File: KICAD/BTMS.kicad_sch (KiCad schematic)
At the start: 151 parts, among them J1 Batt_Ballance, J2 AUX_Charge, J3 Battery_IO, J4 Power_Out, J5 BT_LM62, J6 DSKY, J7 PWR_SW, J8 ICSP, J9 Heater, P1 USB_C_Plug, Q1 SSM3K341R, Q2 DMN65D8L, Q3 SSM3K341R, Q4 FDN340P, Q5 FDN340P, Q6 FDN340P, Q7 DMN65D8L, Q8 DMN65D8L, U1 ACS711xLCTR-25AB, U10 BA033CC0FP-E2, U11 AON7522E, U12 AON7522E, U13 LM62CIM3/NOPB, U14 FAN3100TSX, U15 FAN3100TSX, U16 AON7522E, U17 dsPIC30F3011-PT, U18 FT230XQ, U2 AP33771, U3 IS281-4, U4 Q294700DSGR, U5 SCF4030-12-0X, U6 AONR21321, U7 ACS711xLCTR-25AB, U8 IS281-4, U9 IRS2184

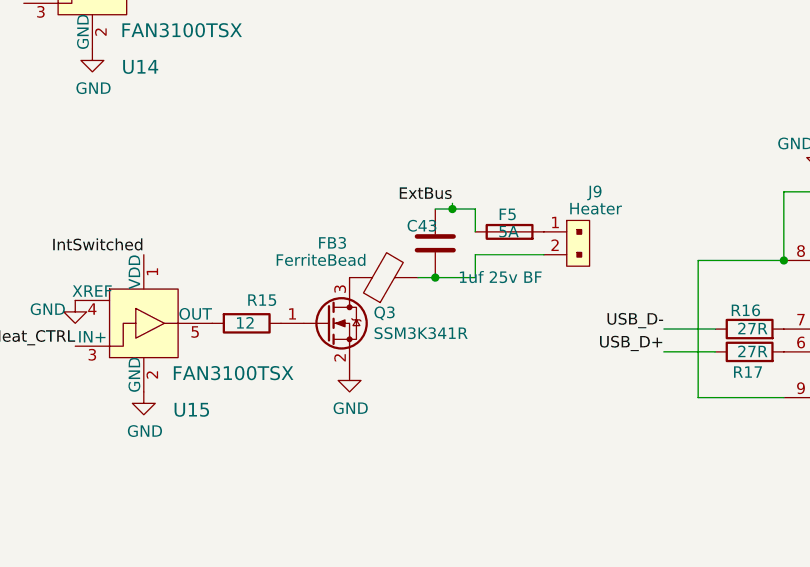
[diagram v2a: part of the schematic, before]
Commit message: Extended board and placed mounting points.
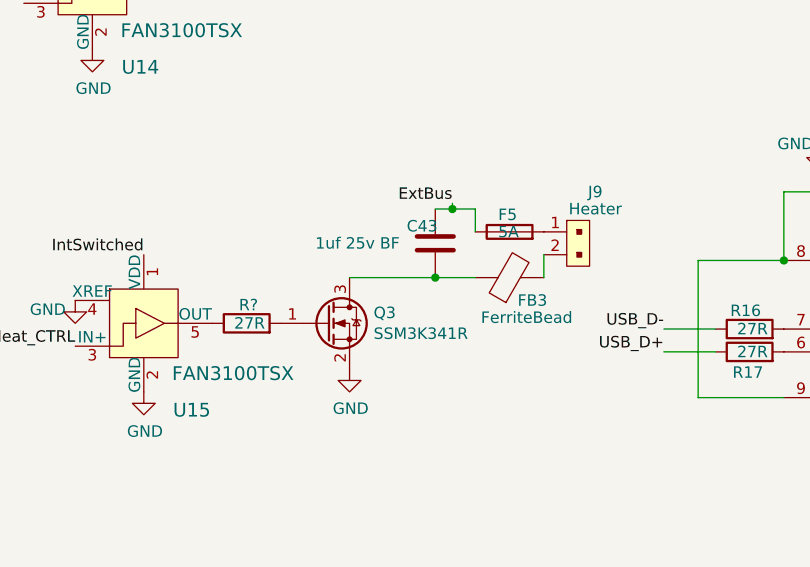
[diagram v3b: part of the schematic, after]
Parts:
- removed R15: 12, Resistor_SMD:R_0603_1608Metric, symbol Device:R
- added R?: 27R, Resistor_SMD:R_0603_1608Metric, symbol Device:R
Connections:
- net at FB3.2, J9.2: no longer C43.2
- net at U15.5 (OUT): now also R?.1
- net at Q3.1 (G): now also R?.2
- net at FB3.1, Q3.3 (D): now also C43.2
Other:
- moved on the sheet: FB3
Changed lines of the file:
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@@
   (junction (at 271.78 39.37) (diameter 0) (color 0 0 0 0)
   )
+  (junction (at 293.37 103.505) (diameter 0) (color 0 0 0 0)
+  )
   (junction (at 249.555 210.185) (diameter 0) (color 0 0 0 0)
   )
@@
   (junction (at 92.71 67.945) (diameter 0) (color 0 0 0 0)
   )
-  (junction (at 293.37 103.505) (diameter 0) (color 0 0 0 0)
-  )
   (junction (at 218.44 208.28) (diameter 0) (color 0 0 0 0)
   )
@@
     (stroke (width 0) (type default) (color 0 0 0 0))
   )
-  (wire (pts (xy 293.37 103.505) (xy 297.815 103.505))
-    (stroke (width 0) (type default) (color 0 0 0 0))
-  )
   (wire (pts (xy 207.645 33.02) (xy 211.455 33.02))
     (stroke (width 0) (type default) (color 0 0 0 0))
@@
     (stroke (width 0) (type default) (color 0 0 0 0))
   )
+  (wire (pts (xy 293.37 103.505) (xy 297.815 103.505))
+    (stroke (width 0) (type default) (color 0 0 0 0))
+  )
   (wire (pts (xy 116.205 214.63) (xy 116.205 231.775))
     (stroke (width 0) (type default) (color 0 0 0 0))
@@
     (stroke (width 0) (type default) (color 0 0 0 0))
   )
+  (wire (pts (xy 283.845 103.505) (xy 293.37 103.505))
+    (stroke (width 0) (type default) (color 0 0 0 0))
+  )
   (wire (pts (xy 83.185 123.825) (xy 94.615 123.825))
     (stroke (width 0) (type default) (color 0 0 0 0))
@@
     (stroke (width 0) (type default) (color 0 0 0 0))
   )
-  (wire (pts (xy 297.815 100.965) (xy 305.435 100.965))
-    (stroke (width 0) (type default) (color 0 0 0 0))
-  )
   (wire (pts (xy 242.57 243.205) (xy 246.38 243.205))
     (stroke (width 0) (type default) (color 0 0 0 0))
@@
     (stroke (width 0) (type default) (color 0 0 0 0))
   )
+  (wire (pts (xy 305.435 100.965) (xy 305.435 103.505))
+    (stroke (width 0) (type default) (color 0 0 0 0))
+  )
   (wire (pts (xy 344.805 20.32) (xy 356.235 20.32))
     (stroke (width 0) (type default) (color 0 0 0 0))
@@
     (stroke (width 0) (type default) (color 0 0 0 0))
   )
-  (wire (pts (xy 291.465 103.505) (xy 293.37 103.505))
-    (stroke (width 0) (type default) (color 0 0 0 0))
-  )
   (wire (pts (xy 83.185 120.015) (xy 83.185 123.825))
     (stroke (width 0) (type default) (color 0 0 0 0))
@@
     (stroke (width 0) (type default) (color 0 0 0 0))
   )
-  (wire (pts (xy 297.815 103.505) (xy 297.815 100.965))
-    (stroke (width 0) (type default) (color 0 0 0 0))
-  )
   (wire (pts (xy 205.105 66.675) (xy 207.645 66.675))
     (stroke (width 0) (type default) (color 0 0 0 0))
@@
     (pin "1")
   )
-  (symbol (lib_id "Device:R") (at 272.415 108.585 270) (unit 1)
-    (in_bom yes) (on_board yes)
-    (property "Reference" "R15" (id 0) (at 272.415 106.045 90)
-      (effects (font (size 1.27 1.27)) (justify left))
-    )
-    (property "Value" "12" (id 1) (at 271.145 108.585 90)
-      (effects (font (size 1.27 1.27)) (justify left))
-    )
-    (property "Footprint" "Resistor_SMD:R_0603_1608Metric" (id 2) (at 272.415 106.807 90)
-      (effects (font (size 1.27 1.27)) hide)
-    )
-    (property "Datasheet" "~" (id 3) (at 272.415 108.585 0)
-      (effects (font (size 1.27 1.27)) hide)
-    )
-    (property "DK_Detail_Page" "https://www.digikey.com/en/products/detail/panasonic-electronic-components/ERJ-UP3J120V/12139275" (id 4) (at 272.415 108.585 0)
-      (effects (font (size 1.27 1.27)) hide)
-    )
-    (property "Digi-Key_PN" "10-ERJ-UP3J120VCT-ND" (id 5) (at 272.415 108.585 0)
-      (effects (font (size 1.27 1.27)) hide)
-    )
-    (pin "1")
-    (pin "2")
-  )
   (symbol (lib_id "Device:R") (at 93.98 20.955 270) (unit 1)
     (in_bom yes) (on_board yes)
@@
       (effects (font (size 1.27 1.27)) (justify left))
     )
-    (property "Value" "1uf 25v BF" (id 1) (at 295.91 103.505 0)
+    (property "Value" "1uf 25v BF" (id 1) (at 280.035 99.695 0)
       (effects (font (size 1.27 1.27)) (justify left))
     )
@@
     (pin "2")
   )
+  (symbol (lib_id "Device:R") (at 272.415 108.585 90) (unit 1)
+    (in_bom yes) (on_board yes)
+    (property "Reference" "R?" (id 0) (at 273.685 106.553 90)
+      (effects (font (size 1.27 1.27)) (justify left))
+    )
+    (property "Value" "27R" (id 1) (at 274.447 108.585 90)
+      (effects (font (size 1.27 1.27)) (justify left))
+    )
+    (property "Footprint" "Resistor_SMD:R_0603_1608Metric" (id 2) (at 272.415 110.363 90)
+      (effects (font (size 1.27 1.27)) hide)
+    )
+    (property "Datasheet" "~" (id 3) (at 272.415 108.585 0)
+      (effects (font (size 1.27 1.27)) hide)
+    )
+    (property "DK_Detail_Page" "https://www.digikey.com/en/products/detail/yageo/RC0603FR-1327RL/14286630" (id 4) (at 272.415 108.585 0)
+      (effects (font (size 1.27 1.27)) hide)
+    )
+    (property "Digi-Key_PN" "13-RC0603FR-1327RLCT-ND" (id 5) (at 272.415 108.585 0)
+      (effects (font (size 1.27 1.27)) hide)
+    )
+    (pin "1")
+    (pin "2")
+  )
   (symbol (lib_id "power:GND") (at 260.985 116.205 0) (unit 1)
     (in_bom yes) (on_board yes)
@@
     (pin "2")
   )
-  (symbol (lib_id "Device:FerriteBead") (at 287.655 103.505 90) (unit 1)
+  (symbol (lib_id "Device:FerriteBead") (at 301.625 103.505 90) (unit 1)
     (in_bom yes) (on_board yes)
-    (property "Reference" "FB3" (id 0) (at 281.94 99.695 90))
-    (property "Value" "FerriteBead" (id 1) (at 280.67 101.6 90))
-    (property "Footprint" "Resistor_SMD:R_1206_3216Metric" (id 2) (at 287.655 105.283 90)
+    (property "Reference" "FB3" (id 0) (at 304.165 106.045 90))
+    (property "Value" "FerriteBead" (id 1) (at 303.53 107.95 90))
+    (property "Footprint" "Resistor_SMD:R_1206_3216Metric" (id 2) (at 301.625 105.283 90)
       (effects (font (size 1.27 1.27)) hide)
     )
-    (property "Datasheet" "~" (id 3) (at 287.655 103.505 0)
+    (property "Datasheet" "~" (id 3) (at 301.625 103.505 0)
       (effects (font (size 1.27 1.27)) hide)
     )
-    (property "DK_Detail_Page" "https://www.digikey.com/en/products/detail/murata-electronics/BLM31SN500SN1L/5881254" (id 4) (at 287.655 103.505 0)
+    (property "DK_Detail_Page" "https://www.digikey.com/en/products/detail/murata-electronics/BLM31SN500SN1L/5881254" (id 4) (at 301.625 103.505 0)
       (effects (font (size 1.27 1.27)) hide)
     )
-    (property "Digi-Key_PN" "490-13269-1-ND" (id 5) (at 287.655 103.505 0)
+    (property "Digi-Key_PN" "490-13269-1-ND" (id 5) (at 301.625 103.505 0)
       (effects (font (size 1.27 1.27)) hide)
     )
@@
       (reference "R14") (unit 1) (value "12") (footprint "Resistor_SMD:R_0603_1608Metric")
     )
-    (path "/3b36b429-3994-44b4-904d-74e991ca114c"
-      (reference "R15") (unit 1) (value "12") (footprint "Resistor_SMD:R_0603_1608Metric")
-    )
     (path "/26e7321b-39c7-46e7-b3a0-1de446d5bd59"
       (reference "R16") (unit 1) (value "27R") (footprint "Resistor_SMD:R_0603_1608Metric")
@@
       (reference "R24") (unit 1) (value "10K") (footprint "Resistor_SMD:R_0603_1608Metric")
     )
+    (path "/a9d1f6bc-926a-4206-95e1-10bfe156bf35"
+      (reference "R?") (unit 1) (value "27R") (footprint "Resistor_SMD:R_0603_1608Metric")
+    )
     (path "/6d1558b7-32bb-4234-9884-0300df2238db"

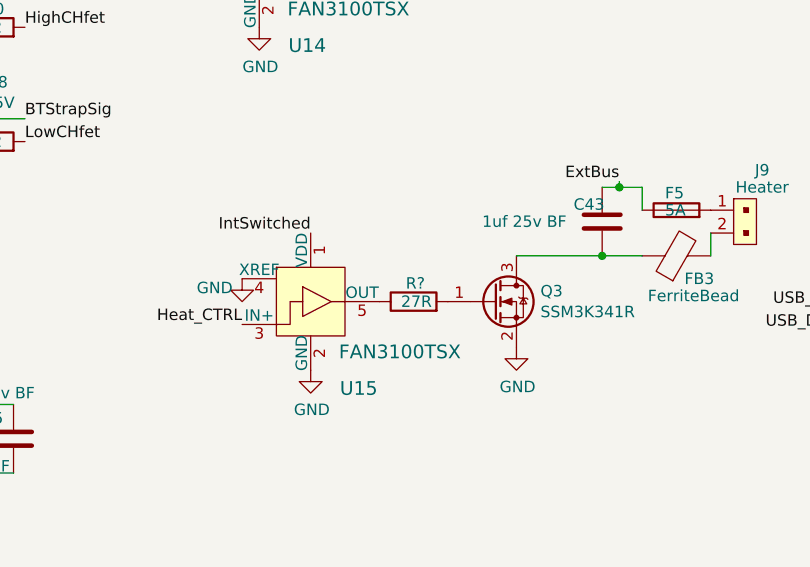
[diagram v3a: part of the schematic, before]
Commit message: Cleaned up connector silkscreens. No more DRC warnings.
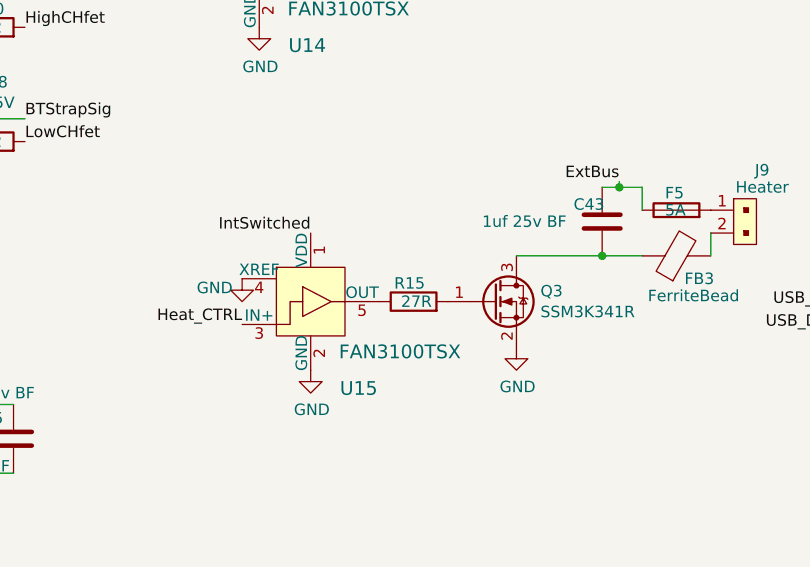
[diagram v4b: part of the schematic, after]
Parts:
- gave numbers to parts that had none: 1
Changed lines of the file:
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@@
   (symbol (lib_id "Device:R") (at 272.415 108.585 90) (unit 1)
     (in_bom yes) (on_board yes)
-    (property "Reference" "R?" (id 0) (at 273.685 106.553 90)
+    (property "Reference" "R15" (id 0) (at 273.685 106.553 90)
       (effects (font (size 1.27 1.27)) (justify left))
     )
@@
       (reference "R14") (unit 1) (value "12") (footprint "Resistor_SMD:R_0603_1608Metric")
     )
+    (path "/a9d1f6bc-926a-4206-95e1-10bfe156bf35"
+      (reference "R15") (unit 1) (value "27R") (footprint "Resistor_SMD:R_0603_1608Metric")
+    )
     (path "/26e7321b-39c7-46e7-b3a0-1de446d5bd59"
       (reference "R16") (unit 1) (value "27R") (footprint "Resistor_SMD:R_0603_1608Metric")
@@
       (reference "R24") (unit 1) (value "10K") (footprint "Resistor_SMD:R_0603_1608Metric")
     )
-    (path "/a9d1f6bc-926a-4206-95e1-10bfe156bf35"
-      (reference "R?") (unit 1) (value "27R") (footprint "Resistor_SMD:R_0603_1608Metric")
-    )
     (path "/6d1558b7-32bb-4234-9884-0300df2238db"

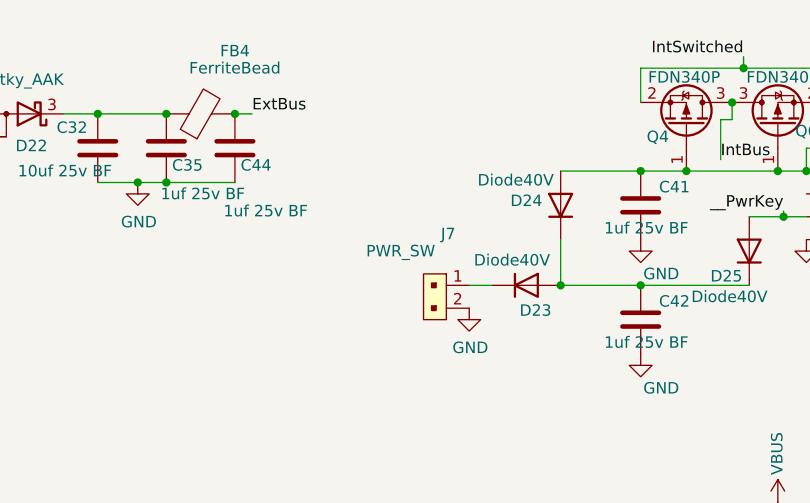
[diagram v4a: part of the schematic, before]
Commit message: Added power switch button. Added credits and description silkscreening.
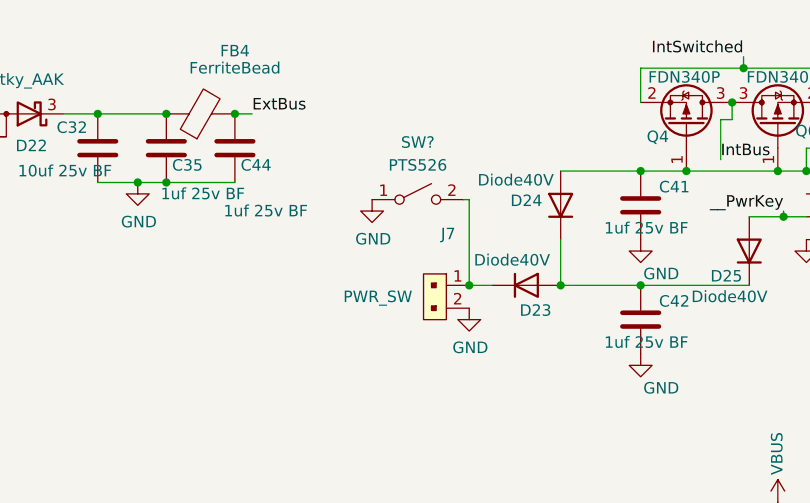
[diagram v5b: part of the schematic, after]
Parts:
- added SW?: PTS526, Button_Switch_SMD:SW_SPST_SKQG_WithStem, symbol Switch:SW_SPST
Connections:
- net GND: now also SW?.1 (A)
- net at D23.1 (K), J7.1: now also SW?.2 (B)
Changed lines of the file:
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@@
   (junction (at 194.945 120.015) (diameter 0) (color 0 0 0 0)
   )
+  (junction (at 325.755 44.45) (diameter 0) (color 0 0 0 0)
+  )
   (junction (at 161.925 25.4) (diameter 0) (color 0 0 0 0)
   )
@@
     (stroke (width 0) (type default) (color 0 0 0 0))
   )
+  (wire (pts (xy 325.755 34.925) (xy 325.755 44.45))
+    (stroke (width 0) (type default) (color 0 0 0 0))
+  )
   (wire (pts (xy 305.435 100.965) (xy 305.435 103.505))
     (stroke (width 0) (type default) (color 0 0 0 0))
@@
     (stroke (width 0) (type default) (color 0 0 0 0))
   )
+  (wire (pts (xy 325.12 34.925) (xy 325.755 34.925))
+    (stroke (width 0) (type default) (color 0 0 0 0))
+  )
   (wire (pts (xy 218.44 205.74) (xy 218.44 208.28))
     (stroke (width 0) (type default) (color 0 0 0 0))
@@
     (in_bom yes) (on_board yes)
     (property "Reference" "J7" (id 0) (at 323.4182 38.735 90))
-    (property "Value" "PWR_SW" (id 1) (at 318.135 40.64 90))
+    (property "Value" "PWR_SW" (id 1) (at 315.595 45.72 90))
     (property "Footprint" "Connector_PinHeader_2.54mm:PinHeader_1x02_P2.54mm_Vertical" (id 2) (at 328.295 49.53 0)
       (effects (font (size 1.524 1.524)) (justify left) hide)
@@
     (pin "2")
   )
+  (symbol (lib_id "Switch:SW_SPST") (at 320.04 34.925 0) (unit 1)
+    (in_bom yes) (on_board yes) (fields_autoplaced)
+    (property "Reference" "SW?" (id 0) (at 320.04 28.575 0))
+    (property "Value" "PTS526" (id 1) (at 320.04 31.115 0))
+    (property "Footprint" "Button_Switch_SMD:SW_SPST_SKQG_WithStem" (id 2) (at 320.04 34.925 0)
+      (effects (font (size 1.27 1.27)) hide)
+    )
+    (property "Datasheet" "~" (id 3) (at 320.04 34.925 0)
+      (effects (font (size 1.27 1.27)) hide)
+    )
+    (property "DK_Detail_Page" "https://www.digikey.com/en/products/detail/c-k/PTS526-SK15-SMTR2-LFS/10056626" (id 4) (at 320.04 34.925 0)
+      (effects (font (size 1.27 1.27)) hide)
+    )
+    (property "Digi-Key_PN" "CKN12221-1-ND" (id 5) (at 320.04 34.925 0)
+      (effects (font (size 1.27 1.27)) hide)
+    )
+    (pin "1")
+    (pin "2")
+  )
   (symbol (lib_id "Device:D_Schottky_AAK") (at 276.86 25.4 180) (unit 1)
     (in_bom yes) (on_board yes)
@@
     (pin "1")
   )
+  (symbol (lib_id "power:GND") (at 314.96 34.925 0) (unit 1)
+    (in_bom yes) (on_board yes)
+    (property "Reference" "#PWR?" (id 0) (at 314.96 41.275 0)
+      (effects (font (size 1.27 1.27)) hide)
+    )
+    (property "Value" "GND" (id 1) (at 315.087 39.3192 0))
+    (property "Footprint" "" (id 2) (at 314.96 34.925 0)
+      (effects (font (size 1.27 1.27)) hide)
+    )
+    (property "Datasheet" "" (id 3) (at 314.96 34.925 0)
+      (effects (font (size 1.27 1.27)) hide)
+    )
+    (pin "1")
+  )
   (symbol (lib_id "Device:D") (at 159.385 175.26 90) (unit 1)
     (in_bom yes) (on_board yes)
@@
       (reference "#PWR0105") (unit 1) (value "GND") (footprint "")
     )
+    (path "/765cf6f4-9db5-4d66-8293-e4e2a047eae9"
+      (reference "#PWR?") (unit 1) (value "GND") (footprint "")
+    )
     (path "/64c76206-53c0-4f04-b9c5-7beac0937b65"
       (reference "C1") (unit 1) (value "0.1uf film") (footprint "Capacitor_SMD:C_0603_1608Metric")
@@
       (reference "RN11") (unit 1) (value "10K") (footprint "Resistor_SMD:R_Array_Convex_4x1206")
     )
+    (path "/67647a8b-db66-4202-969a-7d17a16bd4a5"
+      (reference "SW?") (unit 1) (value "PTS526") (footprint "Button_Switch_SMD:SW_SPST_SKQG_WithStem")
+    )
     (path "/3202d53d-0910-47b2-a7db-5c708ae895e8"

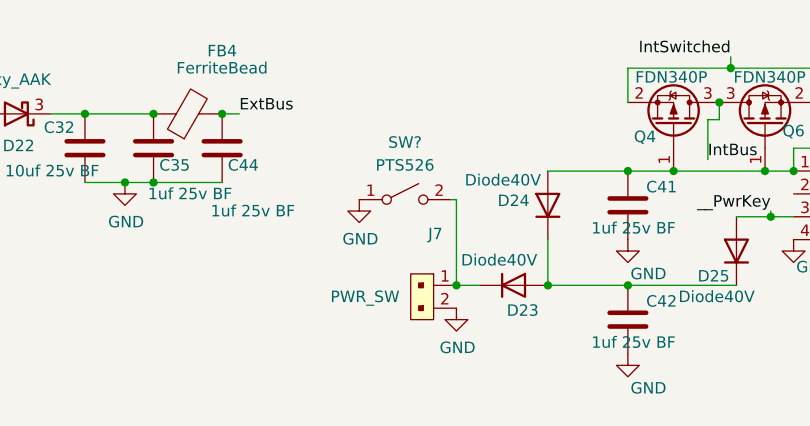
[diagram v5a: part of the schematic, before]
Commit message: Added parts list order.
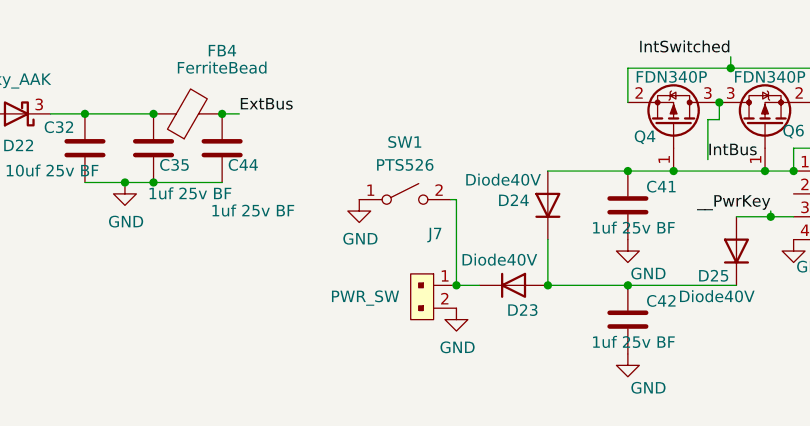
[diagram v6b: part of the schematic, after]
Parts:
- gave numbers to parts that had none: 1
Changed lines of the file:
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@@
   (symbol (lib_id "Switch:SW_SPST") (at 320.04 34.925 0) (unit 1)
     (in_bom yes) (on_board yes) (fields_autoplaced)
-    (property "Reference" "SW?" (id 0) (at 320.04 28.575 0))
+    (property "Reference" "SW1" (id 0) (at 320.04 28.575 0))
     (property "Value" "PTS526" (id 1) (at 320.04 31.115 0))
     (property "Footprint" "Button_Switch_SMD:SW_SPST_SKQG_WithStem" (id 2) (at 320.04 34.925 0)
@@
   (symbol (lib_id "power:GND") (at 314.96 34.925 0) (unit 1)
     (in_bom yes) (on_board yes)
-    (property "Reference" "#PWR?" (id 0) (at 314.96 41.275 0)
+    (property "Reference" "#PWR0106" (id 0) (at 314.96 41.275 0)
       (effects (font (size 1.27 1.27)) hide)
     )
@@
     )
     (path "/765cf6f4-9db5-4d66-8293-e4e2a047eae9"
-      (reference "#PWR?") (unit 1) (value "GND") (footprint "")
+      (reference "#PWR0106") (unit 1) (value "GND") (footprint "")
     )
     (path "/64c76206-53c0-4f04-b9c5-7beac0937b65"
@@
     )
     (path "/67647a8b-db66-4202-969a-7d17a16bd4a5"
-      (reference "SW?") (unit 1) (value "PTS526") (footprint "Button_Switch_SMD:SW_SPST_SKQG_WithStem")
+      (reference "SW1") (unit 1) (value "PTS526") (footprint "Button_Switch_SMD:SW_SPST_SKQG_WithStem")
     )
     (path "/3202d53d-0910-47b2-a7db-5c708ae895e8"
